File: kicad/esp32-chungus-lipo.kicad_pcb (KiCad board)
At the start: 2 copper layers, 25.6 x 44.5 mm, 23 parts, among them J1 USB_B_Micro, J2 Conn_01x02, J3 Conn_01x11, J4 Conn_01x11, U1 ESP32-S3-WROOM-1, U2 MAX1551EZK+T, U3 RT9080-33GJ5, U4 WS2812B

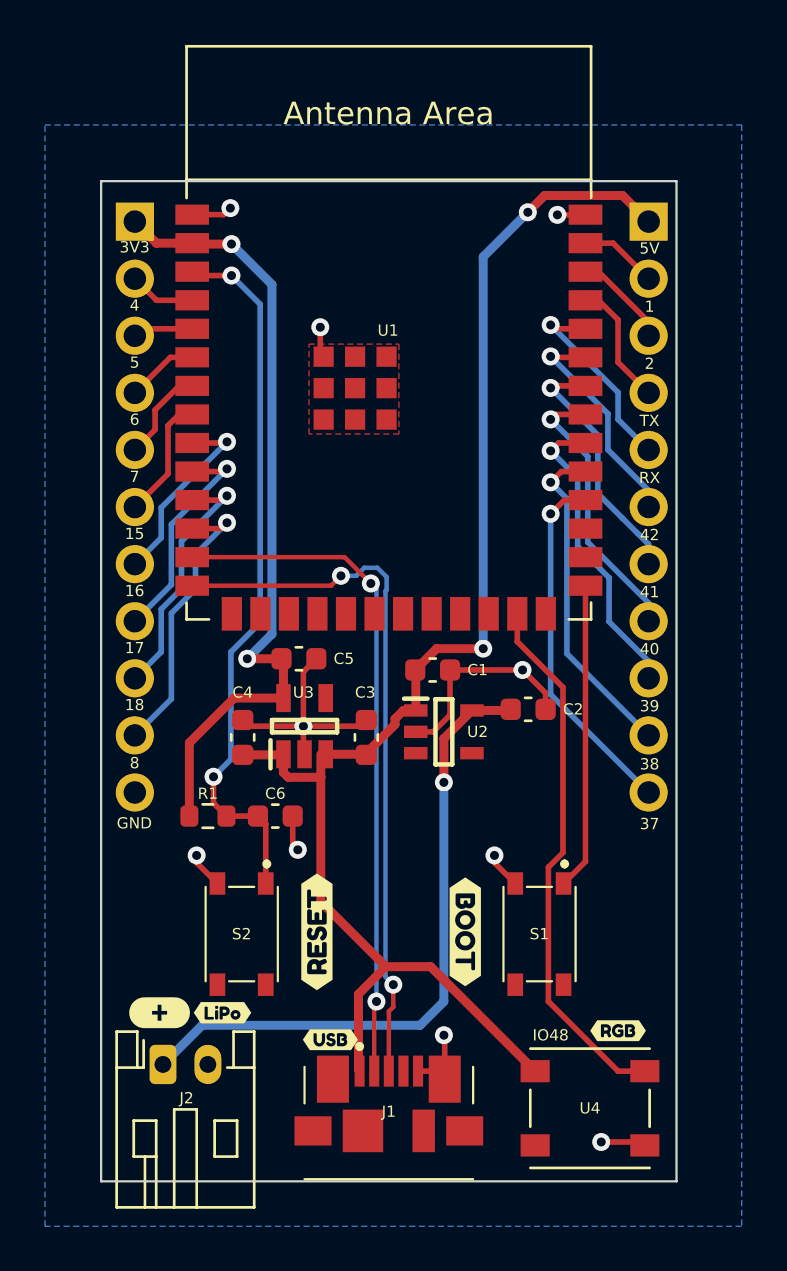
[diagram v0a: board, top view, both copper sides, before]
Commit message: add r2 lipo with fix to power circuit
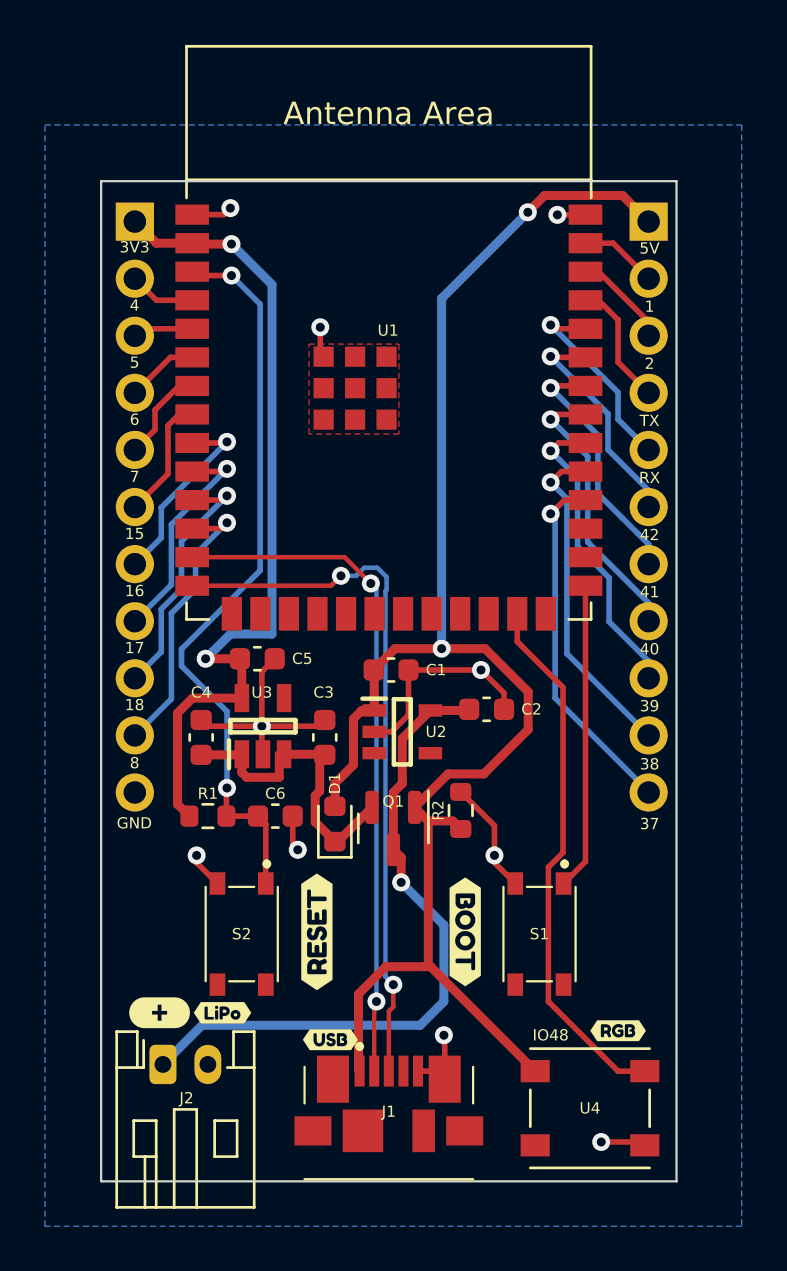
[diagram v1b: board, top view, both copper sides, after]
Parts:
- added D1: 1N5819W, Diode_SMD:D_0603_1608Metric, F.Cu at (130.4, 118.6)
- added G***: LOGO, chungus:chungus, B.Cu at (132.8, 112.0)
- added Q1: CJ2301, Package_TO_SOT_SMD:SOT-23, F.Cu at (133.0, 118.8)
- added R2: 100k, Resistor_SMD:R_0603_1608Metric, F.Cu at (136.0, 118.0)
- moved C3 1.85 mm to (129.9, 114.8)
- moved C5 1.85 mm to (127.0, 111.2)
- moved U3 1.85 mm to (127.2, 114.2)
- moved C1 1.85 mm to (132.9, 111.8)
- moved C2 1.85 mm to (137.2, 113.5)
- moved C4 1.85 mm to (124.5, 114.8)
- moved U2 1.85 mm to (133.4, 114.5)
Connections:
- C3 pad 1: +5V -> Net-(C3-Pad1)
- C4 pad 1: +5V -> Net-(C3-Pad1)
- U3 pad 1: +5V -> Net-(C3-Pad1)
- U3 pad 3: +5V -> Net-(C3-Pad1)
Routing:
- net Net-(C3-Pad1): track 0.00 -> 14.1 mm
- net +5V: track 65.4 -> 73.2 mm
- net GND: track 34.1 -> 37.5 mm
- net +3.3V: track 35.9 -> 37.5 mm
- net /EN: track 32.0 -> 33.2 mm
- net /BAT+: track 28.9 -> 30.0 mm
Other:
- board text added: "ESP Chungus LiPo r2 by ayan4m1"
- board text removed: "ESP Chungus LiPo r1 by ayan4m1"
